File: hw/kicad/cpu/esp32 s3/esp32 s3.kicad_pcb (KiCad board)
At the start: 2 copper layers, 45 x 45 mm, 40 parts, among them J1 TOP, J2 BUTTOM, J3 USB_B_Micro, SW1 SW_Push, U1 ESP32-S3-WROOM-1-N16R2, U2 ICM-42688-P

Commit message: 更新CPU板
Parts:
- added R19: R, Resistor_SMD:R_0603_1608Metric, F.Cu at (87.4, 55.4)
- added R20: R, Resistor_SMD:R_0603_1608Metric, F.Cu at (87.4, 53.9)
- R1, R29, R30: footprint Resistor_SMD:R_0805_2012Metric -> Resistor_SMD:R_0603_1608Metric
- R10, R11, R12, R13, R14, R15, R16, R17, R18, R21, R22, R23, R24, R25, R26, R27, R28, R3, R4, R5, R6, R7, R8, R9: value 100 -> R
- SW1: footprint Button_Switch_SMD:SW_DIP_SPSTx01_Slide_6.7x4.1mm_W6.73mm_P2.54mm_LowProfile_JPin -> Button_Switch_THT:SW_SPST_Omron_B3F-315x_Angled
- moved R1 33.6 mm to (59.9, 38.3), turned to 0 degrees
- moved SW1 32.8 mm to (57.6, 35.3), turned to 0 degrees
- moved D1 28.0 mm to (33.9, 46.3)
- moved R2 28.0 mm to (34.1, 43.7)
- moved R3 23.9 mm to (62.4, 41.9), turned to 180 degrees
- moved R29 22.6 mm to (41.8, 65.5)
- moved R27 22.5 mm to (87.4, 43.2), turned to 0 degrees
- moved R30 20.9 mm to (41.8, 63.8)
- moved R5 20.6 mm to (62.4, 44.9), turned to 180 degrees
- moved R28 20.5 mm to (87.4, 41.7), turned to 0 degrees
- moved R25 19.2 mm to (87.4, 46.3), turned to 0 degrees
- moved J3 19.0 mm to (36.4, 55.5)
- moved R4 19.0 mm to (62.4, 43.4), turned to 180 degrees
- moved R26 17.3 mm to (87.4, 44.8), turned to 0 degrees
- moved C1 16.9 mm to (44.7, 42.4), turned to 90 degrees
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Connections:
- J1 pad 10: /UART3_Tx -> /I2C_CLK
- J1 pad 11: /I2C_SDA -> /SPI_CS
- J1 pad 12: /I2C_CLK -> /SPI_CLK
- J1 pad 13: /SPI_CS -> /SPI_MOSI
- J1 pad 14: /SPI_CLK -> /SPI_MISO
- J1 pad 15: /SPI_MOSI -> /GPIO_1
- J1 pad 16: /SPI_MISO -> /GPIO_2
- J1 pad 17: /GPIO_1 -> /GPIO_3
- J1 pad 18: /GPIO_2 -> /GPIO_4
- J1 pad 19: /GPIO_3 -> /GPIO_5
- J1 pad 20: /GPIO_4 -> /GPIO_6
- J1 pad 21: /GPIO_5 -> /GPIO_7
- J1 pad 22: /GPIO_6 -> /GPIO_8
- J1 pad 23: /GPIO_7 -> /GPIO_9
- J1 pad 24: /GPIO_8 -> /GPIO_10
- J1 pad 25: /GPIO_9 -> /GPIO_11
- J1 pad 26: /GPIO_10 -> /GPIO_12
- J1 pad 9: /UART3_Rx -> /I2C_SDA
- J2 pad 10: /UART3_Rx -> /I2C_SDA
- J2 pad 11: /I2C_CLK -> /SPI_CLK
- J2 pad 12: /I2C_SDA -> /SPI_CS
- J2 pad 13: /SPI_CLK -> /SPI_MISO
- J2 pad 14: /SPI_CS -> /SPI_MOSI
- J2 pad 15: /SPI_MISO -> /GPIO_2
- J2 pad 16: /SPI_MOSI -> /GPIO_1
- J2 pad 17: /GPIO_2 -> /GPIO_4
- J2 pad 18: /GPIO_1 -> /GPIO_3
- J2 pad 19: /GPIO_4 -> /GPIO_6
- J2 pad 20: /GPIO_3 -> /GPIO_5
- J2 pad 21: /GPIO_6 -> /GPIO_8
- J2 pad 22: /GPIO_5 -> /GPIO_7
- J2 pad 23: /GPIO_8 -> /GPIO_10
- J2 pad 24: /GPIO_7 -> /GPIO_9
- J2 pad 25: /GPIO_10 -> /GPIO_12
- J2 pad 26: /GPIO_9 -> /GPIO_11
- J2 pad 9: /UART3_Tx -> /I2C_CLK
- R1 pad 1: GND -> Net-(R1-Pad1)
- R1 pad 2: Net-(R1-Pad2) -> Net-(U1-IO0)
- R10 pad 2: /UART2_TX -> /UART2_Tx
- R11 pad 1: /i2c_clk -> /i2c_sda
- R12 pad 1: /i2c_sda -> /i2c_clk
- R17 pad 1: /gpio9 -> /gpio1
- R17 pad 2: /GPIO_9 -> /GPIO_1
- R18 pad 1: /gpio10 -> /gpio2
- R18 pad 2: /GPIO_10 -> /GPIO_2
- R21 pad 1: /gpio1 -> /gpio5
- R21 pad 2: /GPIO_1 -> /GPIO_5
- R22 pad 1: /gpio2 -> /gpio6
- R22 pad 2: /GPIO_2 -> /GPIO_6
- R23 pad 1: /gpio3 -> /gpio7
- R23 pad 2: /GPIO_3 -> /GPIO_7
- R24 pad 1: /gpio4 -> /gpio8
- R24 pad 2: /GPIO_4 -> /GPIO_8
- R25 pad 1: /gpio5 -> /gpio9
- R25 pad 2: /GPIO_5 -> /GPIO_9
- R26 pad 1: /gpio5 -> /gpio10
- R26 pad 2: /GPIO_6 -> /GPIO_10
- R27 pad 1: /gpio7 -> /gpio11
- R27 pad 2: /GPIO_7 -> /GPIO_11
- R28 pad 1: /gpio8 -> /gpio12
- R28 pad 2: /GPIO_8 -> /GPIO_12
- R29 pad 2: /USB+ -> /usb+
- R30 pad 2: /USB- -> /usb-
- R7 pad 2: /UART1_RX -> /UART1_Rx
- R8 pad 2: /UART1_TX -> /UART1_Tx
- R9 pad 2: /UART2_RX -> /UART2_Rx
- SW1 pad 1: Net-(R1-Pad2) -> GND
- SW1 pad 2: Net-(U1-IO0) -> Net-(R1-Pad1)
- U1 pad 10: /i2c_clk -> unconnected-(U1-IO17-Pad10)
- U1 pad 11: /i2c_sda -> unconnected-(U1-IO18-Pad11)
- U1 pad 13: /usb_d- -> /usb-
- U1 pad 14: /usb_d+ -> /usb+
- U1 pad 17: /spi2_cs -> /uart1_rx
- U1 pad 18: /spi2_mosi -> /uart1_tx
- U1 pad 19: /spi2_clk -> /i2c_sda
- U1 pad 20: /spi2_miso -> /i2c_clk
- U1 pad 23: /spi3_mosi -> /spi3_miso
- U1 pad 24: /spi3_miso -> /spi3_mosi
- U1 pad 25: /IMU_FSYNC -> /gpio1
- U1 pad 26: unconnected-(U1-IO45-Pad26) -> /gpio2
- U1 pad 28: /gpio1 -> /gpio3
- U1 pad 29: /gpio2 -> /gpio4
- U1 pad 30: /gpio3 -> /gpio5
- U1 pad 31: /gpio4 -> /gpio6
- U1 pad 32: /gpio5 -> /gpio7
- U1 pad 33: /gpio5 -> /gpio8
- U1 pad 34: /gpio7 -> /gpio9
- U1 pad 35: /gpio8 -> /gpio10
- U1 pad 38: /gpio9 -> /gpio11
- U1 pad 39: /gpio10 -> /gpio12
- U1 pad 8: /uart1_tx -> unconnected-(U1-IO15-Pad8)
- U1 pad 9: /uart1_rx -> unconnected-(U1-IO16-Pad9)
- U2 pad 1: /spi3_miso -> /spi2_miso
- U2 pad 12: /spi3_cs -> /spi2_cs
- U2 pad 13: /spi3_clk -> /spi2_clk
- U2 pad 14: /spi3_mosi -> /spi2_mosi
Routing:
- net /UART3_Tx: vias 2 -> 0
- net /UART3_Rx: vias 2 -> 0
- net /UART2_Tx: vias 2 -> 1
- net /GPIO_12: vias 0 -> 2
- net /GPIO_11: vias 0 -> 2
- net /ADC_4: vias 2 -> 1
- net /ADC_3: vias 2 -> 1

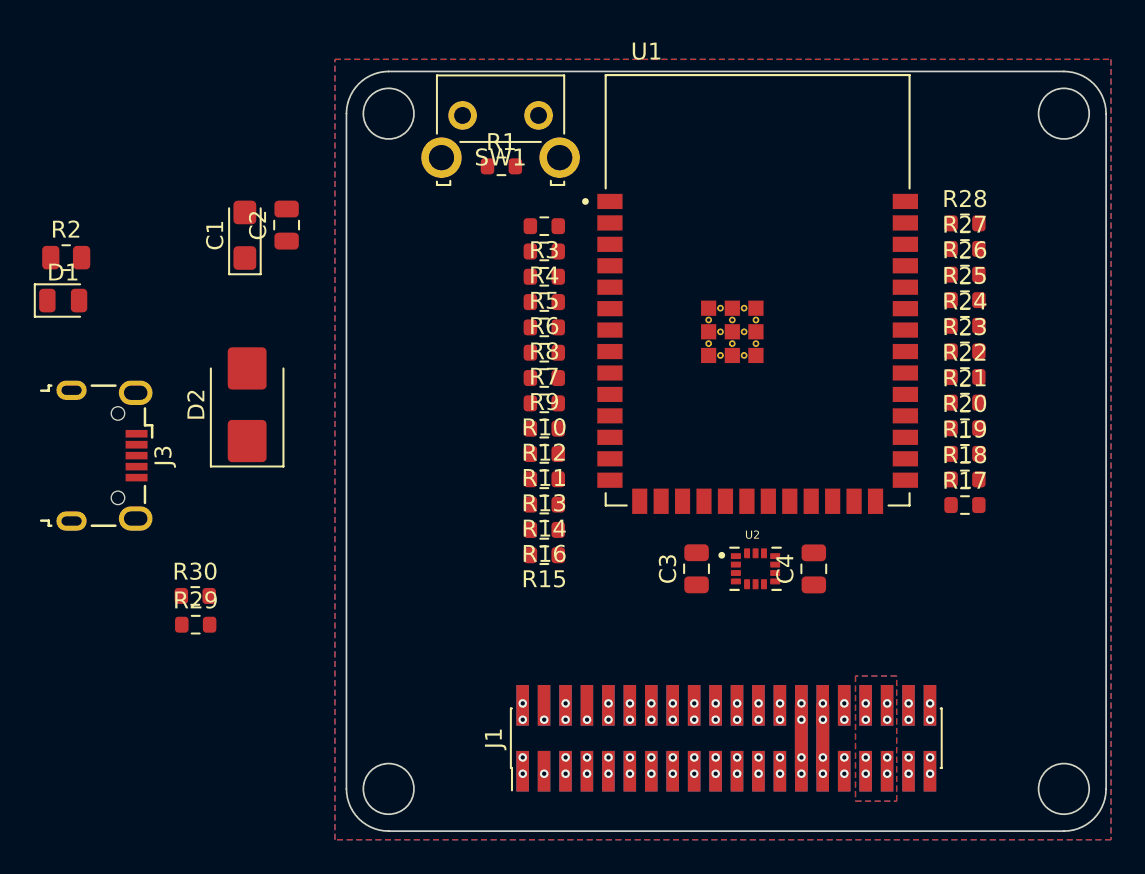
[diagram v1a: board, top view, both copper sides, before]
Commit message: 更新ESP32 S3 CPU板
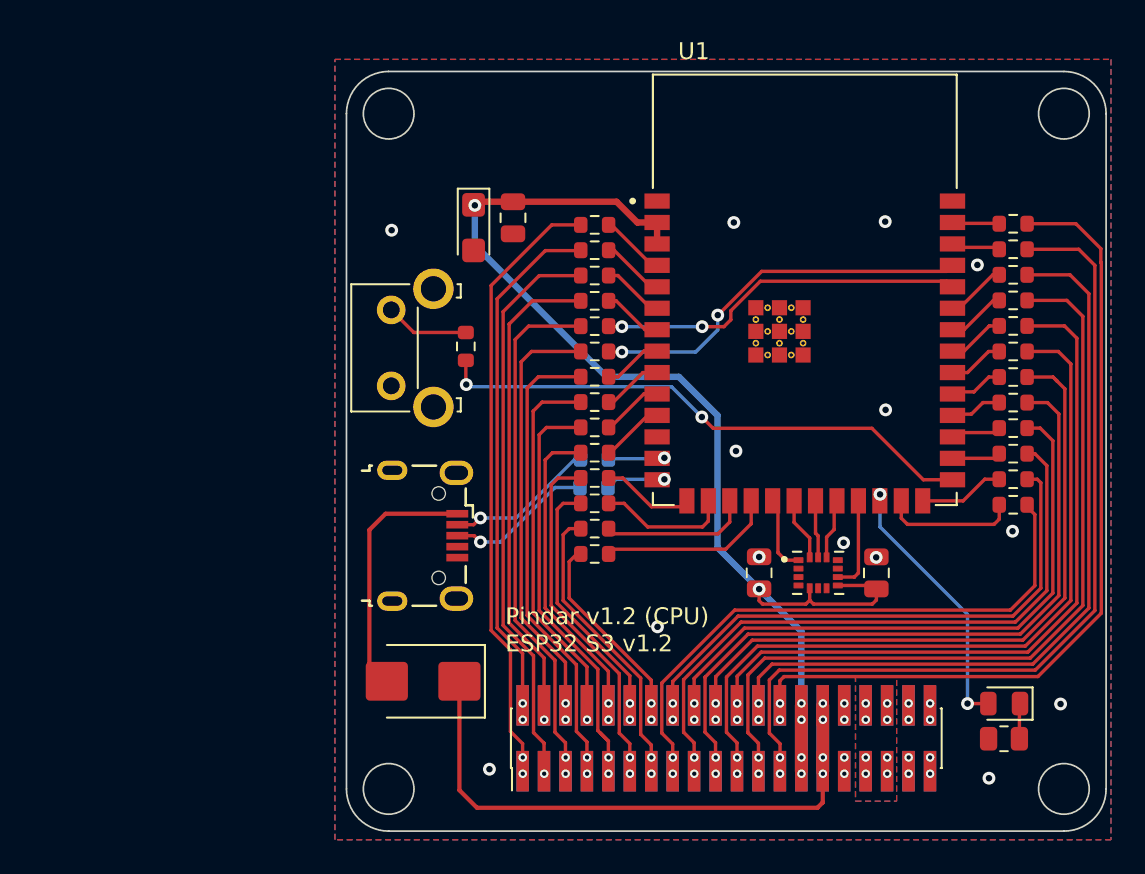
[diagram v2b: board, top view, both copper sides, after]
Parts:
- R29, R30: moved to B.Cu
- moved R2 62.4 mm to (89.7, 72.2)
- moved D1 60.6 mm to (89.7, 70.2), turned to 180 degrees
- moved R30 25.0 mm to (65.4, 55.7)
- moved R29 25.0 mm to (65.4, 57.4)
- moved J3 19.6 mm to (55.4, 60.2)
- moved D2 19.4 mm to (55.3, 68.8), turned to 180 degrees
- moved SW1 16.6 mm to (53.4, 51.3), turned to 90 degrees
- moved C1 13.6 mm to (58.2, 42.0), turned to -90 degrees
- moved C2 13.4 mm to (60.6, 41.4), turned to -90 degrees
- moved R1 10.9 mm to (57.8, 49.0), turned to -90 degrees
- moved U2 3.72 mm to (78.7, 62.4)
- moved C3 3.72 mm to (75.2, 62.4)
- moved C4 3.72 mm to (82.1, 62.4)
- moved R11 3.37 mm to (65.4, 53.8)
- moved R15 3.37 mm to (65.4, 59.8)
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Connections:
- U1 pad 10: unconnected-(U1-IO17-Pad10) -> /i2c_sda
- U1 pad 11: unconnected-(U1-IO18-Pad11) -> /i2c_clk
- U1 pad 12: /LED -> unconnected-(U1-IO8-Pad12)
- U1 pad 15: unconnected-(U1-IO3-Pad15) -> /spi3_cs
- U1 pad 16: unconnected-(U1-IO46-Pad16) -> /spi3_clk
- U1 pad 17: /uart1_rx -> /spi3_mosi
- U1 pad 18: /uart1_tx -> /spi3_miso
- U1 pad 19: /i2c_sda -> /spi2_miso
- U1 pad 20: /i2c_clk -> /spi2_mosi
- U1 pad 21: /spi3_cs -> /spi2_clk
- U1 pad 22: /spi3_clk -> /spi2_cs
- U1 pad 23: /spi3_miso -> /IMU_FSYNC
- U1 pad 24: /spi3_mosi -> /LED
- U1 pad 41_10: (no net) -> GND
- U1 pad 41_11: (no net) -> GND
- U1 pad 41_12: (no net) -> GND
- U1 pad 41_13: (no net) -> GND
- U1 pad 41_14: (no net) -> GND
- U1 pad 41_15: (no net) -> GND
- U1 pad 41_16: (no net) -> GND
- U1 pad 41_17: (no net) -> GND
- U1 pad 41_18: (no net) -> GND
- U1 pad 41_19: (no net) -> GND
- U1 pad 41_20: (no net) -> GND
- U1 pad 41_21: (no net) -> GND
- U1 pad 8: unconnected-(U1-IO15-Pad8) -> /uart1_rx
- U1 pad 9: unconnected-(U1-IO16-Pad9) -> /uart1_tx
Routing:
- net +3.3V: track 7.80 -> 72.4 mm, vias 4 -> 6
- net /GPIO_11: track 0.00 -> 50.7 mm
- net /GPIO_12: track 0.00 -> 48.7 mm
- net /GPIO_9: track 0.00 -> 48.3 mm
- net /GPIO_10: track 0.00 -> 45.7 mm
- net /GPIO_7: track 0.00 -> 45.0 mm
- net /GPIO_8: track 0.00 -> 42.5 mm
- net /GPIO_5: track 0.00 -> 41.7 mm
- net /GPIO_6: track 0.00 -> 39.3 mm
- net /GPIO_3: track 0.00 -> 38.3 mm
- net /ADC_1: track 0.00 -> 36.3 mm
- net /GPIO_4: track 0.00 -> 35.8 mm
- net /GPIO_1: track 0.00 -> 35.0 mm
- net /ADC_3: track 0.00 -> 33.7 mm
- net /GPIO_2: track 0.00 -> 32.7 mm
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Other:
- board text added: "Pindar v1.2 (CPU) ESP32 S3 v1.2"
